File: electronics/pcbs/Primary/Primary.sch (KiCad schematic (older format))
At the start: 26 parts, among them J1 Line Sensor 1, J11 I2C Bus, J12 Battery, J13 Pololu_D24V50F5, J14 Magnet, J2 Line Sensor 2, J3 Line Sensor 3, J4 Line Sensor 4, J5 Line Sensor 5, J6 Line Sensor 6, J7 Servo, J8 Pololu_DRV8834, J9 Stepper Motor, P1 Digital, P10 CONN_01X01, P11 CONN_01X01, P12 CONN_01X01, P13 CONN_01X01, P2 Power, P3 Analog, P4 Analog, P5 PWM, P6 PWM, P7 Communication, P8 CONN_01X01, P9 CONN_01X01

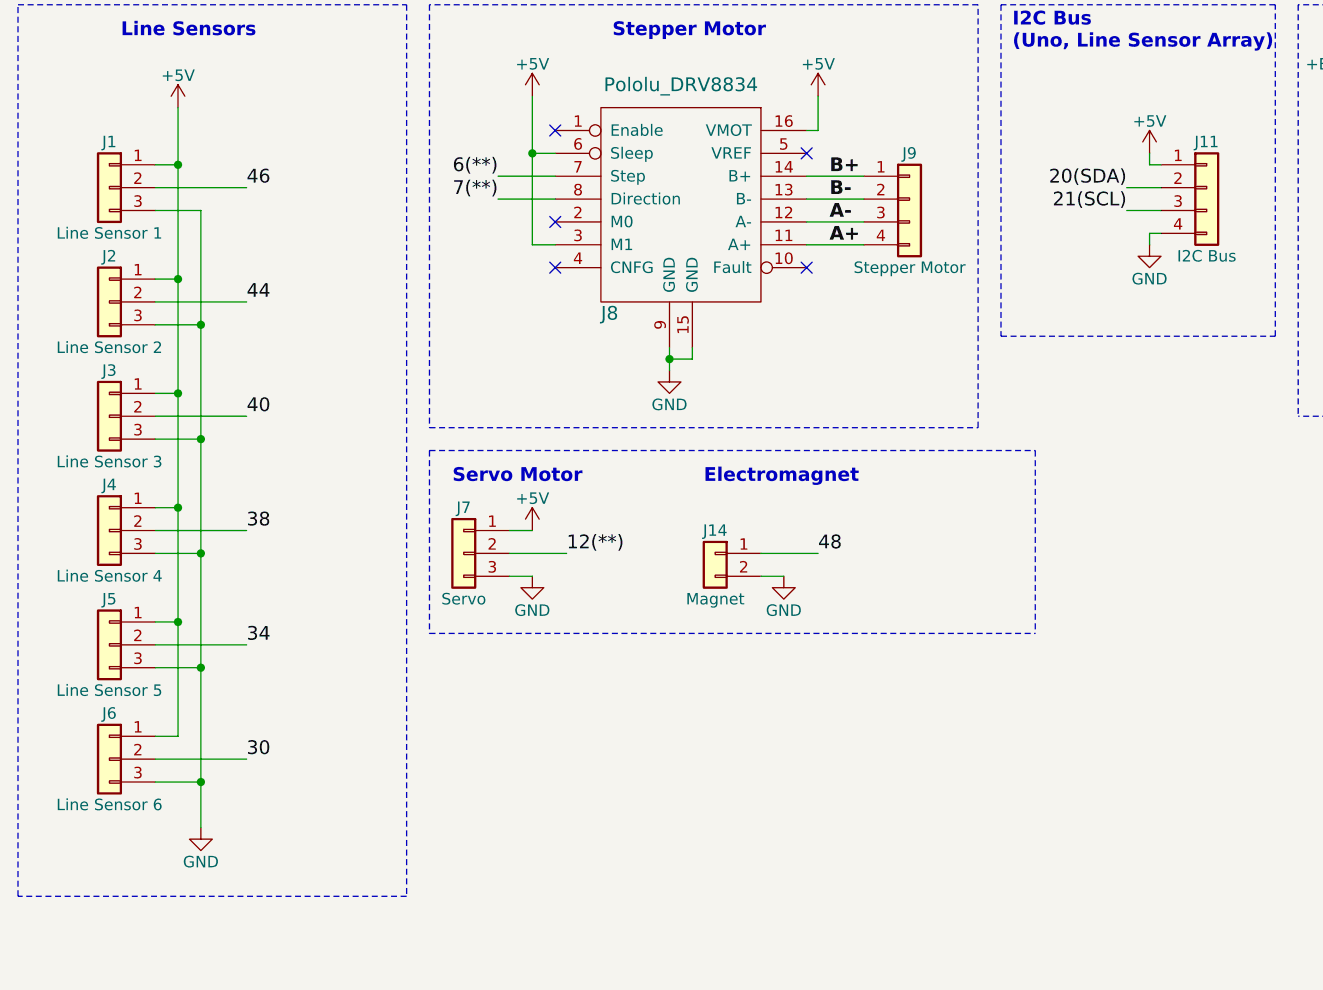
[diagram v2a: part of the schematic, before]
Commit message: Primary/Motor PCBs: Rearranged the GND pin on breakout headers so that we can avoid needing two layers. This change makes the boards more easily prototyped using hobbyist tools like the OtherMill, where plating holes and vias is difficult.
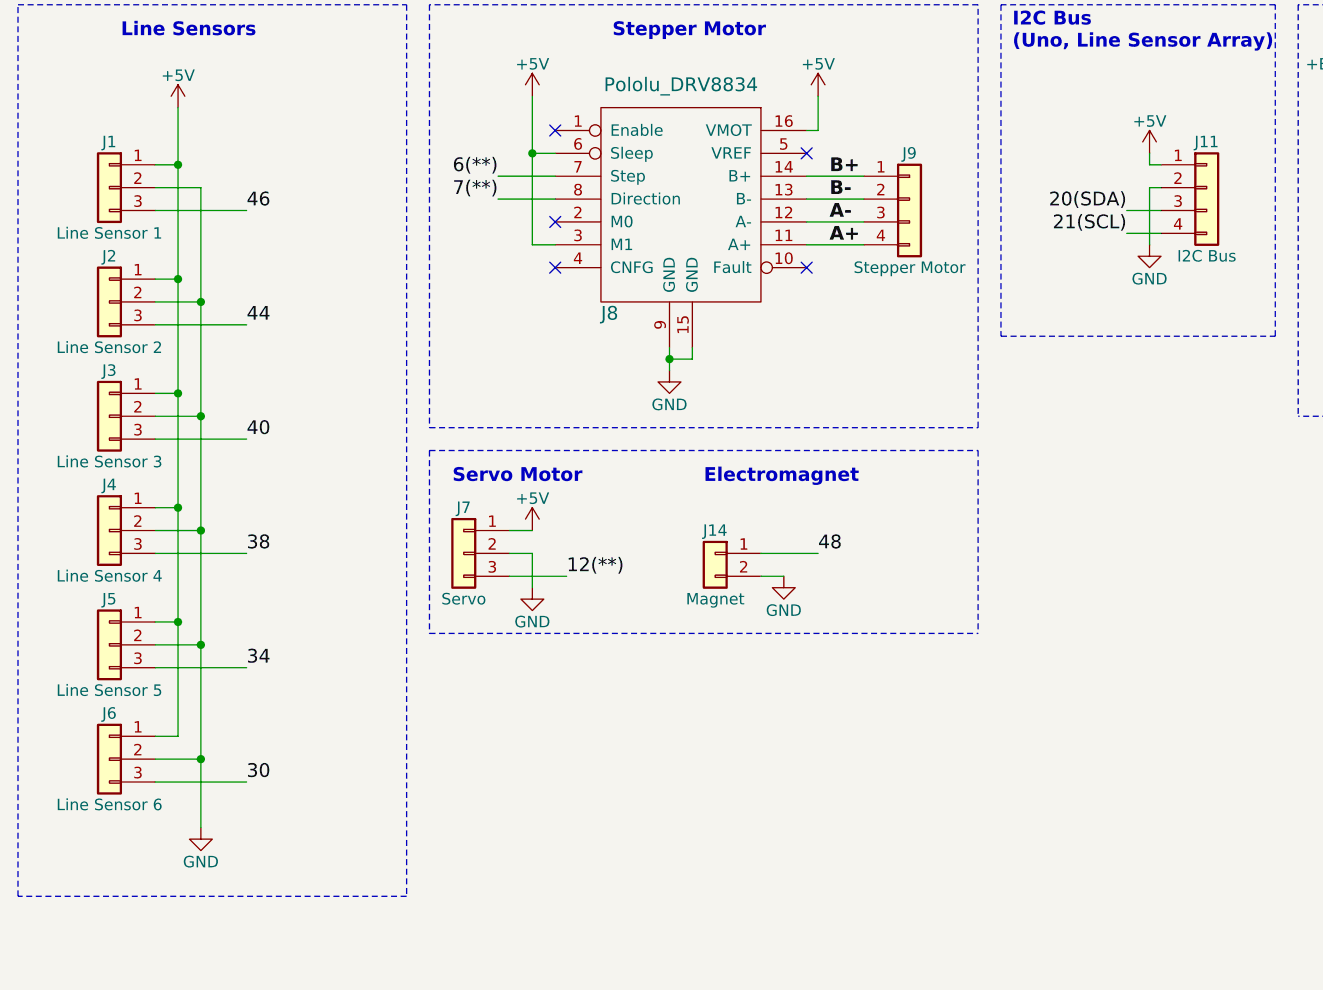
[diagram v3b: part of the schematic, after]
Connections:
- net 12(**): now also J7.3 (Pin_3); no longer J7.2 (Pin_2)
- net 20(SDA): now also J11.3 (Pin_3); no longer J11.2 (Pin_2)
- net 21(SCL): now also J11.4 (Pin_4); no longer J11.3 (Pin_3)
- net 30: now also J6.3 (Pin_3); no longer J6.2 (Pin_2)
- net 34: now also J5.3 (Pin_3); no longer J5.2 (Pin_2)
- net 38: now also J4.3 (Pin_3); no longer J4.2 (Pin_2)
- net 40: now also J3.3 (Pin_3); no longer J3.2 (Pin_2)
- net 44: now also J2.3 (Pin_3); no longer J2.2 (Pin_2)
- net 46: now also J1.3 (Pin_3); no longer J1.2 (Pin_2)
- net GND: now also J1.2 (Pin_2), J11.2 (Pin_2), J2.2 (Pin_2), J3.2 (Pin_2), J4.2 (Pin_2), J5.2 (Pin_2), J6.2 (Pin_2), J7.2 (Pin_2); no longer J1.3 (Pin_3), J11.4 (Pin_4), J2.3 (Pin_3), J3.3 (Pin_3), J4.3 (Pin_3), J5.3 (Pin_3), J6.3 (Pin_3), J7.3 (Pin_3)
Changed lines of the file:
@@
 Text Notes 5650 750  0    60   ~ 12
 I2C Bus\n(Uno, Line Sensor Array)
-Text Label 6150 1350 2    60   ~ 0
+Text Label 6150 1450 2    60   ~ 0
 20(SDA)
-Text Label 6150 1450 2    60   ~ 0
+Text Label 6150 1550 2    60   ~ 0
 21(SCL)
 Wire Wire Line
@@
 Connection ~ 2000 3250
 Wire Wire Line
-	1900 1450 2100 1450
-Wire Wire Line
-	2100 1450 2100 4150
-Wire Wire Line
-	1900 3950 2100 3950
-Connection ~ 2100 3950
-Wire Wire Line
-	1900 3450 2100 3450
-Connection ~ 2100 3450
-Wire Wire Line
-	1900 2950 2100 2950
-Connection ~ 2100 2950
-Wire Wire Line
-	1900 2450 2100 2450
-Connection ~ 2100 2450
-Wire Wire Line
-	1900 1950 2100 1950
-Connection ~ 2100 1950
-Wire Wire Line
-	1900 1350 2300 1350
-Wire Wire Line
-	1900 1850 2300 1850
-Wire Wire Line
-	1900 2350 2300 2350
-Wire Wire Line
-	1900 2850 2300 2850
-Wire Wire Line
-	1900 3350 2300 3350
-Wire Wire Line
-	1900 3850 2300 3850
+	2100 1350 2100 4150
+Connection ~ 2100 3850
+Connection ~ 2100 3350
+Connection ~ 2100 2850
+Connection ~ 2100 2350
+Connection ~ 2100 1850
 Wire Notes Line
 	1300 550  3000 550
@@
 	6250 1250 6300 1250
 Wire Wire Line
-	6300 1550 6250 1550
-Wire Wire Line
-	6250 1550 6250 1600
+	6250 1350 6250 1600
 Wire Notes Line
 	6800 550  5600 550
@@
 L GND #PWR014
 U 1 1 5AB1284A
-P 3550 3050
-F 0 "#PWR014" H 3550 2800 50  0001 C CNN
-F 1 "GND" H 3550 2900 50  0000 C CNN
-F 2 "" H 3550 3050 50  0000 C CNN
-F 3 "" H 3550 3050 50  0000 C CNN
-	1    3550 3050
-	1    0    0    -1
-$EndComp
-Wire Wire Line
-	3450 3050 3550 3050
+P 3550 3100
+F 0 "#PWR014" H 3550 2850 50  0001 C CNN
+F 1 "GND" H 3550 2950 50  0000 C CNN
+F 2 "" H 3550 3100 50  0000 C CNN
+F 3 "" H 3550 3100 50  0000 C CNN
+	1    3550 3100
+	1    0    0    -1
+$EndComp
 Wire Wire Line
 	3550 2850 3450 2850
-Wire Wire Line
-	3450 2950 3700 2950
 Wire Notes Line
 	3100 2500 3100 3300
 Wire Notes Line
-	3100 3300 5750 3300
-Wire Notes Line
-	3100 2500 5750 2500
+	3100 3300 5500 3300
+Wire Notes Line
+	3100 2500 5500 2500
 $Comp
 L Pololu_D24V50F5 J13
@@
 	4550 2950 4800 2950
 Wire Notes Line
-	5750 2500 5750 3300
+	5500 2500 5500 3300
 Text Label 4850 1300 0    60   ~ 12
 B+
@@
 Text Label 3400 1400 2    60   ~ 0
 7(**)
-Text Label 3700 2950 0    60   ~ 0
+Text Label 3700 3050 0    60   ~ 0
 12(**)
 Text Label 4800 2950 0    60   ~ 0
 48
-Text Label 2300 1350 0    60   ~ 0
+Text Label 2300 1450 0    60   ~ 0
 46
-Text Label 2300 1850 0    60   ~ 0
+Text Label 2300 1950 0    60   ~ 0
 44
-Text Label 2300 3850 0    60   ~ 0
+Text Label 2300 3950 0    60   ~ 0
 30
-Text Label 2300 3350 0    60   ~ 0
+Text Label 2300 3450 0    60   ~ 0
 34
-Text Label 2300 2850 0    60   ~ 0
+Text Label 2300 2950 0    60   ~ 0
 38
-Text Label 2300 2350 0    60   ~ 0
+Text Label 2300 2450 0    60   ~ 0
 40
 NoConn ~ 9500 4850
@@
 Connection ~ 10900 850
 Connection ~ 11000 850
-Wire Wire Line
-	6150 1350 6300 1350
-Wire Wire Line
-	6300 1450 6150 1450
 $Comp
 L +BATT #PWR029
@@
 	1    0    0    -1
 $EndComp
+Wire Wire Line
+	1900 3850 2100 3850
+Wire Wire Line
+	2100 3350 1900 3350
+Wire Wire Line
+	2100 2850 1900 2850
+Wire Wire Line
+	2100 2350 1900 2350
+Wire Wire Line
+	2100 1850 1900 1850
+Wire Wire Line
+	2100 1350 1900 1350
+Wire Wire Line
+	2300 1450 1900 1450
+Wire Wire Line
+	2300 1950 1900 1950
+Wire Wire Line
+	2300 2450 1900 2450
+Wire Wire Line
+	2300 2950 1900 2950
+Wire Wire Line
+	2300 3450 1900 3450
+Wire Wire Line
+	2300 3950 1900 3950
+Wire Wire Line
+	3450 2950 3550 2950
+Wire Wire Line
+	3550 2950 3550 3100
+Wire Wire Line
+	3700 3050 3450 3050
+Wire Wire Line
+	6250 1350 6300 1350
+Wire Wire Line
+	6150 1450 6300 1450
+Wire Wire Line
+	6300 1550 6150 1550
 $EndSCHEMATC
